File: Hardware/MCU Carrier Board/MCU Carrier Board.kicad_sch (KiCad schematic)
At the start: 0 parts

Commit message: start
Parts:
- added J7, J8: Conn_02x10_Counter_Clockwise, MCU_Controller:HRS_DF40C-20DP-0.4V_51_, symbol MCU_Controller:DF40C-20DP-0.4V_51_
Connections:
- new net GND: J7.12, J7.14, J7.16, J8.16, J8.18, J8.20
- new net GPIO1: J8.11
- new net GPIO10: J7.11
- new net GPIO11: J7.9
- new net GPIO12: J7.7
- new net GPIO13: J7.5
- new net GPIO14: J7.3
- new net GPIO15: J8.10
- new net GPIO16: J8.12
- new net GPIO17: J8.14
- new net GPIO18: J7.19
- new net GPIO2: J8.9
- new net GPIO21: J7.1
- new net GPIO3: J7.15
- new net GPIO35: J8.2
- new net GPIO36: J8.4
- new net GPIO37: J8.6
- new net GPIO38: J8.8
- new net GPIO4: J8.13
- new net GPIO41: J8.1
- new net GPIO42: J8.3
- new net GPIO47: J7.4
- new net GPIO48: J7.2
- new net GPIO5: J8.15
- new net GPIO6: J8.17
- new net GPIO7: J8.19
- new net GPIO8: J7.17
- new net GPIO9: J7.13
- new net RXD0: J8.5
- new net TXD0: J8.7
- new net VCC_3V3: J7.10, J7.6, J7.8
- new net VCC_5V: J7.18, J7.20

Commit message: update
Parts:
- added C1, C3: .1uF, Capacitor_SMD:C_0603_1608Metric_Pad1.08x0.95mm_HandSolder, symbol Device:C
- added C10, C11, C12, C9: 1uF, Capacitor_SMD:C_0603_1608Metric_Pad1.08x0.95mm_HandSolder, symbol Device:C
- added C2, C4: 10uF, Capacitor_SMD:C_0603_1608Metric_Pad1.08x0.95mm_HandSolder, symbol Device:C
- added D4, D5, D6, D7: LED, LED_SMD:LED_0603_1608Metric_Pad1.05x0.95mm_HandSolder, symbol MCU_Controller:LED
- added J2: Conn_01x05_Pin, Connector_JST:JST_EH_S5B-EH_1x05_P2.50mm_Horizontal, symbol MCU_Controller:Conn_01x05_Pin
- added R10, R7, R8, R9: 1K, Resistor_SMD:R_0603_1608Metric_Pad0.98x0.95mm_HandSolder, symbol MCU_Controller:R
- added SW1, SW2, SW3: SW_Push, Button_Switch_SMD:SW_Push_1P1T_XKB_TS-1187A, symbol MCU_Controller:SW_Push
- added SW10, SW11, SW12, SW13, SW14, SW15, SW16, SW5, SW6, SW7, SW8, SW9: SW_Push, Button_Switch_THT:SW_PUSH_6mm, symbol Switch:SW_Push
- added U3: Left Joystick, COM_09032:XDCR_COM-09032, symbol COM-09032:Joystick-09032
- added U4: Right Joystick, COM_09032:XDCR_COM-09032, symbol COM-09032:Joystick-09032
- J7: value Conn_02x10_Counter_Clockwise -> Top Connector; footprint MCU_Controller:HRS_DF40C-20DP-0.4V_51_ -> DF40C:HRS_DF40C-20DS-0.4V_51_; symbol MCU_Controller:DF40C-20DP-0.4V_51_ -> DF40C:DF40C-20DS-0.4V_51_; MANUFACTURER Hirose Electric -> HRS; MAXIMUM_PACKAGE_HEIGHT 1.29mm -> 1.65 mm; PARTREV 02/2020 -> Sept.1.2020
- J8: value Conn_02x10_Counter_Clockwise -> Bottom Connector; footprint MCU_Controller:HRS_DF40C-20DP-0.4V_51_ -> DF40C:HRS_DF40C-20DS-0.4V_51_; symbol MCU_Controller:DF40C-20DP-0.4V_51_ -> DF40C:DF40C-20DS-0.4V_51_; MANUFACTURER Hirose Electric -> HRS; MAXIMUM_PACKAGE_HEIGHT 1.29mm -> 1.65 mm; PARTREV 02/2020 -> Sept.1.2020
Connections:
- net GND: now also J7.11, J7.13, J7.15, J8.15, J8.17, J8.19, C1.1, C10.2, C11.2, C12.2, C2.1, C3.2, C4.2, C9.2, D4.1 (K), D5.1 (K), D6.1 (K), D7.1 (K), J2.3 (Pin_3), SW1.1, SW10.2, SW11.1, SW12.1, SW13.2, SW14.2, SW15.1, SW16.1, SW2.1, SW3.1, SW5.2, SW6.2, SW7.1, SW8.1, SW9.2, U3.B2A (SEL-), U3.H3 (H-), U3.S1 (SHIELD), U3.S2 (SHIELD__1), U3.S3 (SHIELD__2), U3.S4 (SHIELD__3), U3.V3 (V-), U4.B2A (SEL-), U4.H3 (H-), U4.S1 (SHIELD), U4.S2 (SHIELD__1), U4.S3 (SHIELD__2), U4.S4 (SHIELD__3), U4.V3 (V-); no longer J7.12, J7.14, J7.16, J8.16, J8.18, J8.20
- net GPIO1: now also J8.12, C11.1, U4.V2 (V); no longer J8.11
- net GPIO10: now also J7.12, SW16.2; no longer J7.11
- net GPIO11: now also J7.10, SW5.1; no longer J7.9
- net GPIO12: now also J7.8, SW6.1; no longer J7.7
- net GPIO13: now also J7.6, SW7.2; no longer J7.5
- net GPIO14: now also J7.4, SW8.2; no longer J7.3
- net GPIO15: now also J8.9, U4.B1A (SEL+); no longer J8.10
- net GPIO16: now also J8.11, U3.B1A (SEL+); no longer J8.12
- net GPIO17: now also J8.13, SW11.2; no longer J8.14
- net GPIO18: now also J7.20, SW9.1; no longer J7.19
- net GPIO2: now also J8.10, C12.1, U4.H2 (H); no longer J8.9
- net GPIO21: now also J7.2, SW1.2; no longer J7.1
- net GPIO3: now also J7.16, SW12.2; no longer J7.15
- net GPIO35: now also J8.1, R10.1; no longer J8.2
- net GPIO36: now also J8.3, R9.1; no longer J8.4
- net GPIO37: now also J8.5, R8.1; no longer J8.6
- net GPIO38: now also J8.7, R7.1; no longer J8.8
- net GPIO4: now also J8.14, C9.1, U3.V2 (V); no longer J8.13
- net GPIO41: now also J8.2, J2.5 (Pin_5); no longer J8.1
- net GPIO42: now also J8.4, J2.4 (Pin_4); no longer J8.3
- net GPIO47: now also J7.3, SW2.2; no longer J7.4
- net GPIO48: now also J7.1, SW3.2; no longer J7.2
- net GPIO5: now also J8.16, C10.1, U3.H2 (H); no longer J8.15
- net GPIO6: now also J8.18, SW10.1; no longer J8.17
- net GPIO7: now also J8.20, SW13.1; no longer J8.19
- net GPIO8: now also J7.18, SW15.2; no longer J7.17
- net GPIO9: now also J7.14, SW14.1; no longer J7.13
- net RXD0: now also J8.6, J2.2 (Pin_2); no longer J8.5
- net TXD0: now also J8.8, J2.1 (Pin_1); no longer J8.7
- net VCC_3V3: now also J7.5, J7.7, J7.9, C3.1, C4.1, U3.H1 (H+), U3.V1 (V+), U4.H1 (H+), U4.V1 (V+); no longer J7.10, J7.6, J7.8
- net VCC_5V: now also J7.17, J7.19, C1.2, C2.2; no longer J7.18, J7.20
- new net: D5.2 (A), R8.2
- new net: D6.2 (A), R9.2
- new net: D4.2 (A), R7.2
- new net: D7.2 (A), R10.2
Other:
- note added: "I2C"
- note added: "Play Inicater LEDs"
- note added: "Uart"

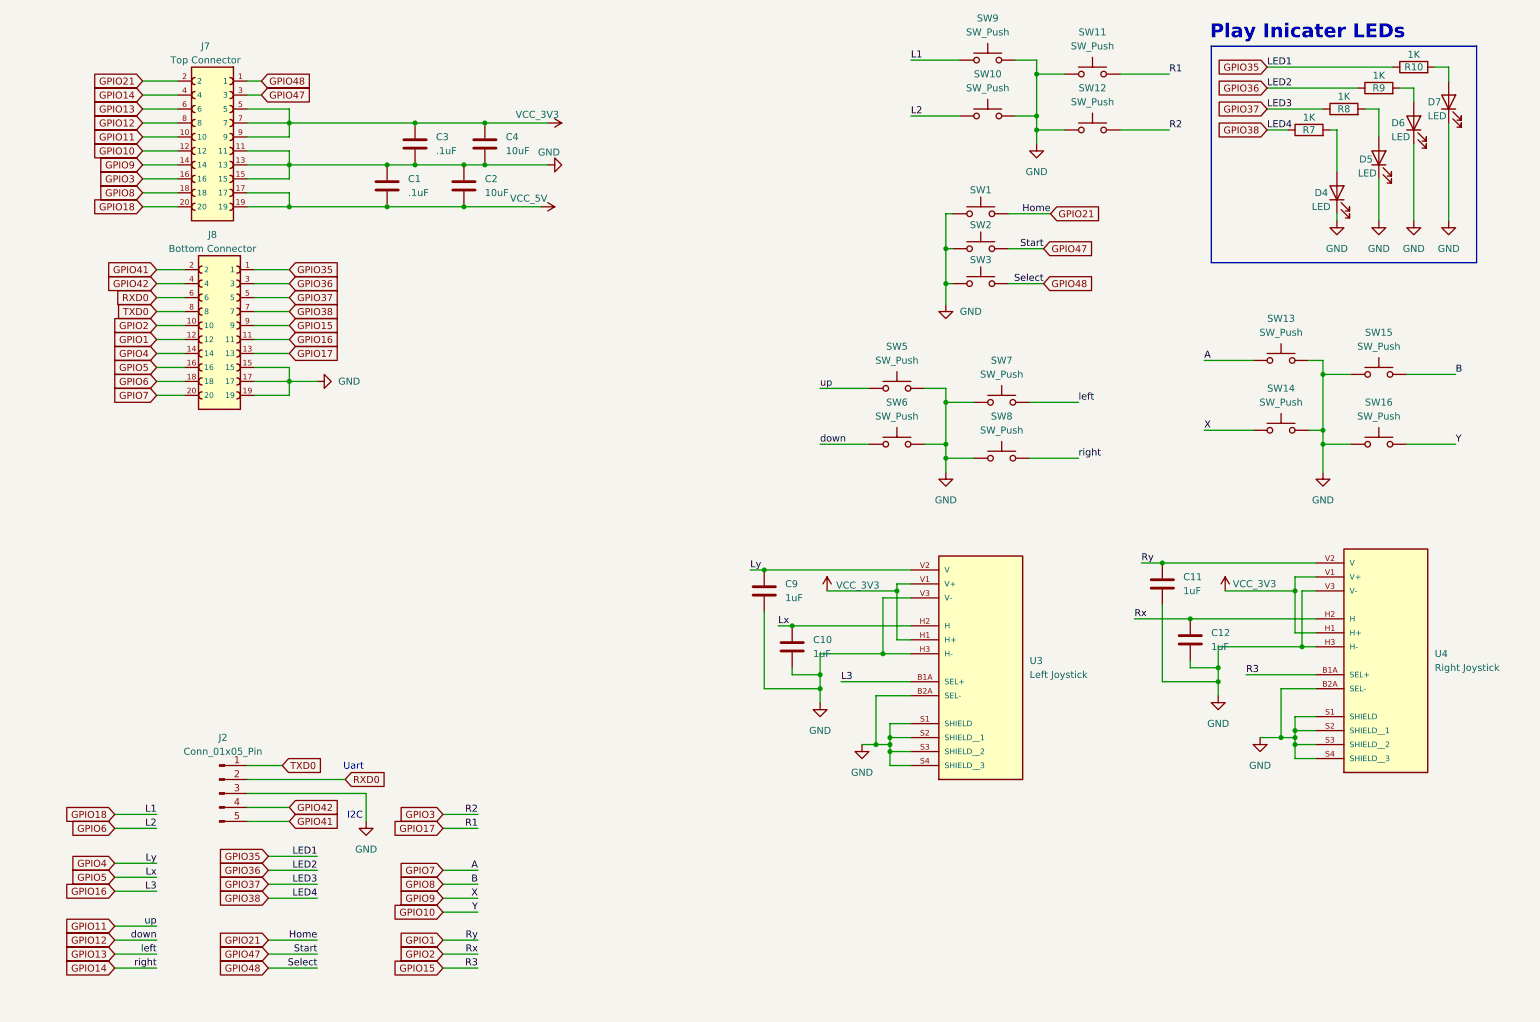
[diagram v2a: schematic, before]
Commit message: locked placement of key components
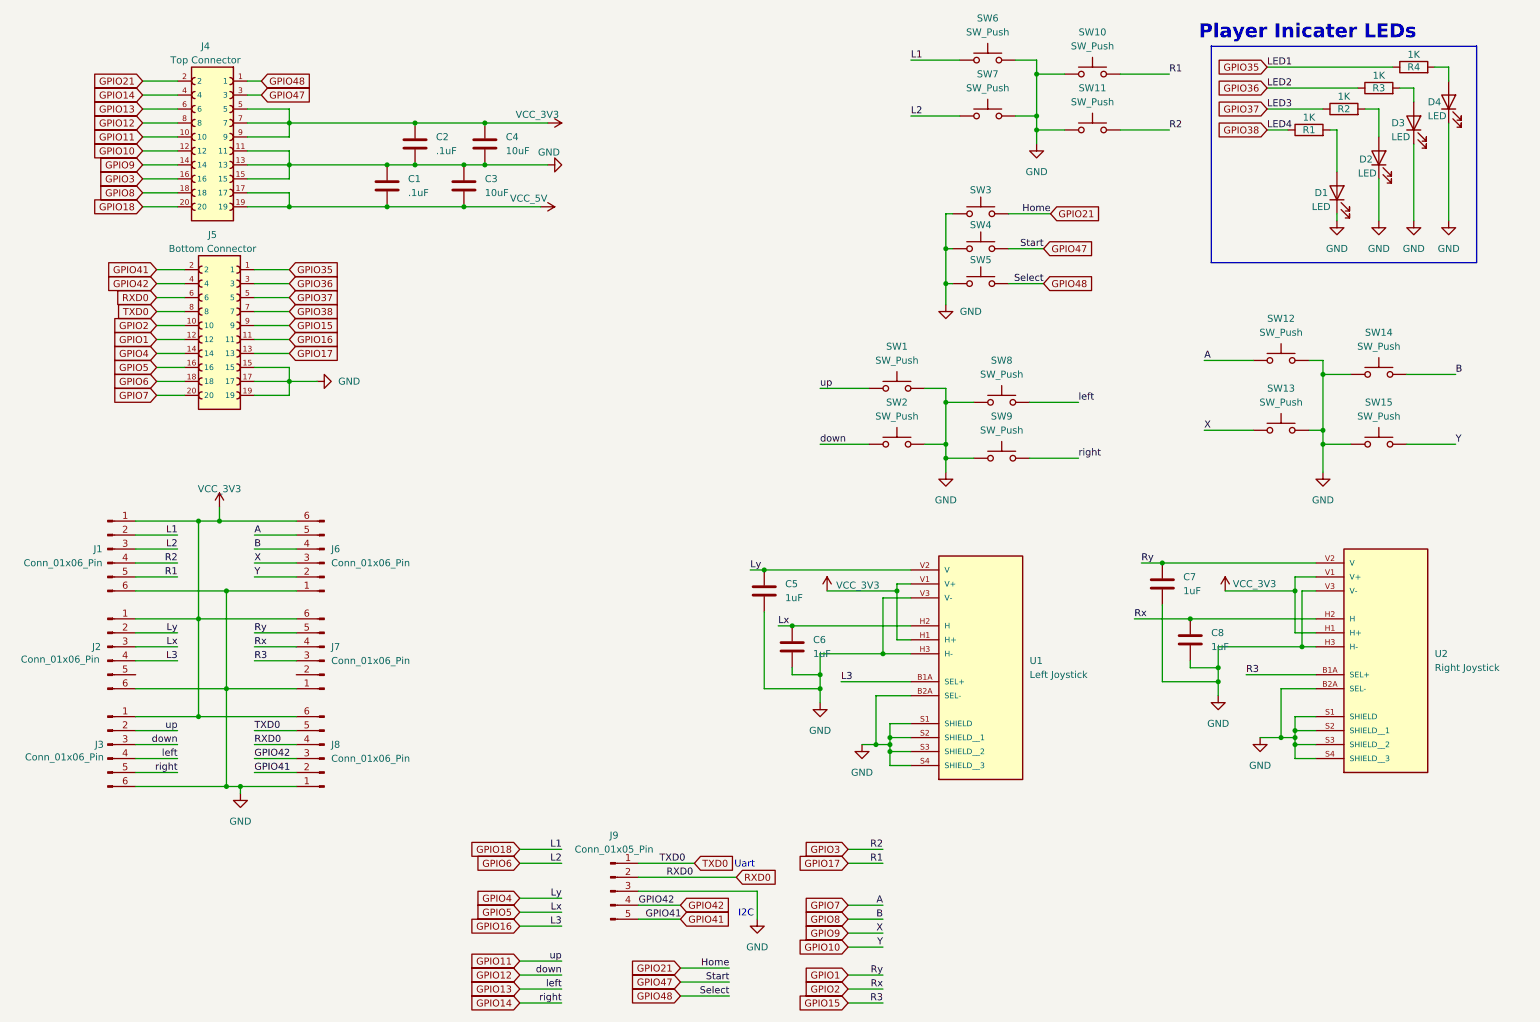
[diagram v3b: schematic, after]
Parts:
- added J1, J2, J3, J6, J7, J8: Conn_01x06_Pin, Connector_PinHeader_1.27mm:PinHeader_1x06_P1.27mm_Vertical, symbol Connector:Conn_01x06_Pin
- C5: renamed from C9; now left out of the parts list
- C6: renamed from C10; now left out of the parts list
- C7: renamed from C11; now left out of the parts list
- C8: renamed from C12; now left out of the parts list
- J9: renamed from J2; now left out of the parts list
- SW1: renamed from SW5; now left out of the parts list
- SW10: renamed from SW11; now left out of the parts list
- SW11: renamed from SW12; now left out of the parts list
- SW12: renamed from SW13; now left out of the parts list
- SW13: renamed from SW14; now left out of the parts list
- SW14: renamed from SW15; now left out of the parts list
- SW15: renamed from SW16; now left out of the parts list
- SW2: renamed from SW6; now left out of the parts list
- SW3: renamed from SW1; now left out of the parts list
- SW4: renamed from SW2; now left out of the parts list
- SW5: renamed from SW3; now left out of the parts list
- SW6: renamed from SW9; now left out of the parts list
- SW7: renamed from SW10; now left out of the parts list
- SW8: renamed from SW7; now left out of the parts list
- SW9: renamed from SW8; now left out of the parts list
- U1: renamed from U3; now left out of the parts list
- U2: renamed from U4; now left out of the parts list
- renumbered C3 to C2, C2 to C3, D4 to D1, D5 to D2, D6 to D3, D7 to D4, J7 to J4, J8 to J5, R7 to R1, R8 to R2, R9 to R3, R10 to R4
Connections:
- net GND: now also J1.6 (Pin_6), J2.6 (Pin_6), J3.6 (Pin_6), J6.1 (Pin_1), J7.1 (Pin_1), J8.1 (Pin_1)
- net GPIO1: now also J7.5 (Pin_5)
- net GPIO10: now also J6.2 (Pin_2)
- net GPIO11: now also J3.2 (Pin_2)
- net GPIO12: now also J3.3 (Pin_3)
- net GPIO13: now also J3.4 (Pin_4)
- net GPIO14: now also J3.5 (Pin_5)
- net GPIO15: now also J7.3 (Pin_3)
- net GPIO16: now also J2.4 (Pin_4)
- net GPIO17: now also J1.5 (Pin_5)
- net GPIO18: now also J1.2 (Pin_2)
- net GPIO2: now also J7.4 (Pin_4)
- net GPIO3: now also J1.4 (Pin_4)
- net GPIO4: now also J2.2 (Pin_2)
- net GPIO41: now also J8.2 (Pin_2)
- net GPIO42: now also J8.3 (Pin_3)
- net GPIO5: now also J2.3 (Pin_3)
- net GPIO6: now also J1.3 (Pin_3)
- net GPIO7: now also J6.5 (Pin_5)
- net GPIO8: now also J6.4 (Pin_4)
- net GPIO9: now also J6.3 (Pin_3)
- net RXD0: now also J8.4 (Pin_4)
- net TXD0: now also J8.5 (Pin_5)
- net VCC_3V3: now also J1.1 (Pin_1), J2.1 (Pin_1), J3.1 (Pin_1), J6.6 (Pin_6), J7.6 (Pin_6), J8.6 (Pin_6)
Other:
- note added: "Player Inicater LEDs"
- note removed: "Play Inicater LEDs"
- moved on the sheet: J9

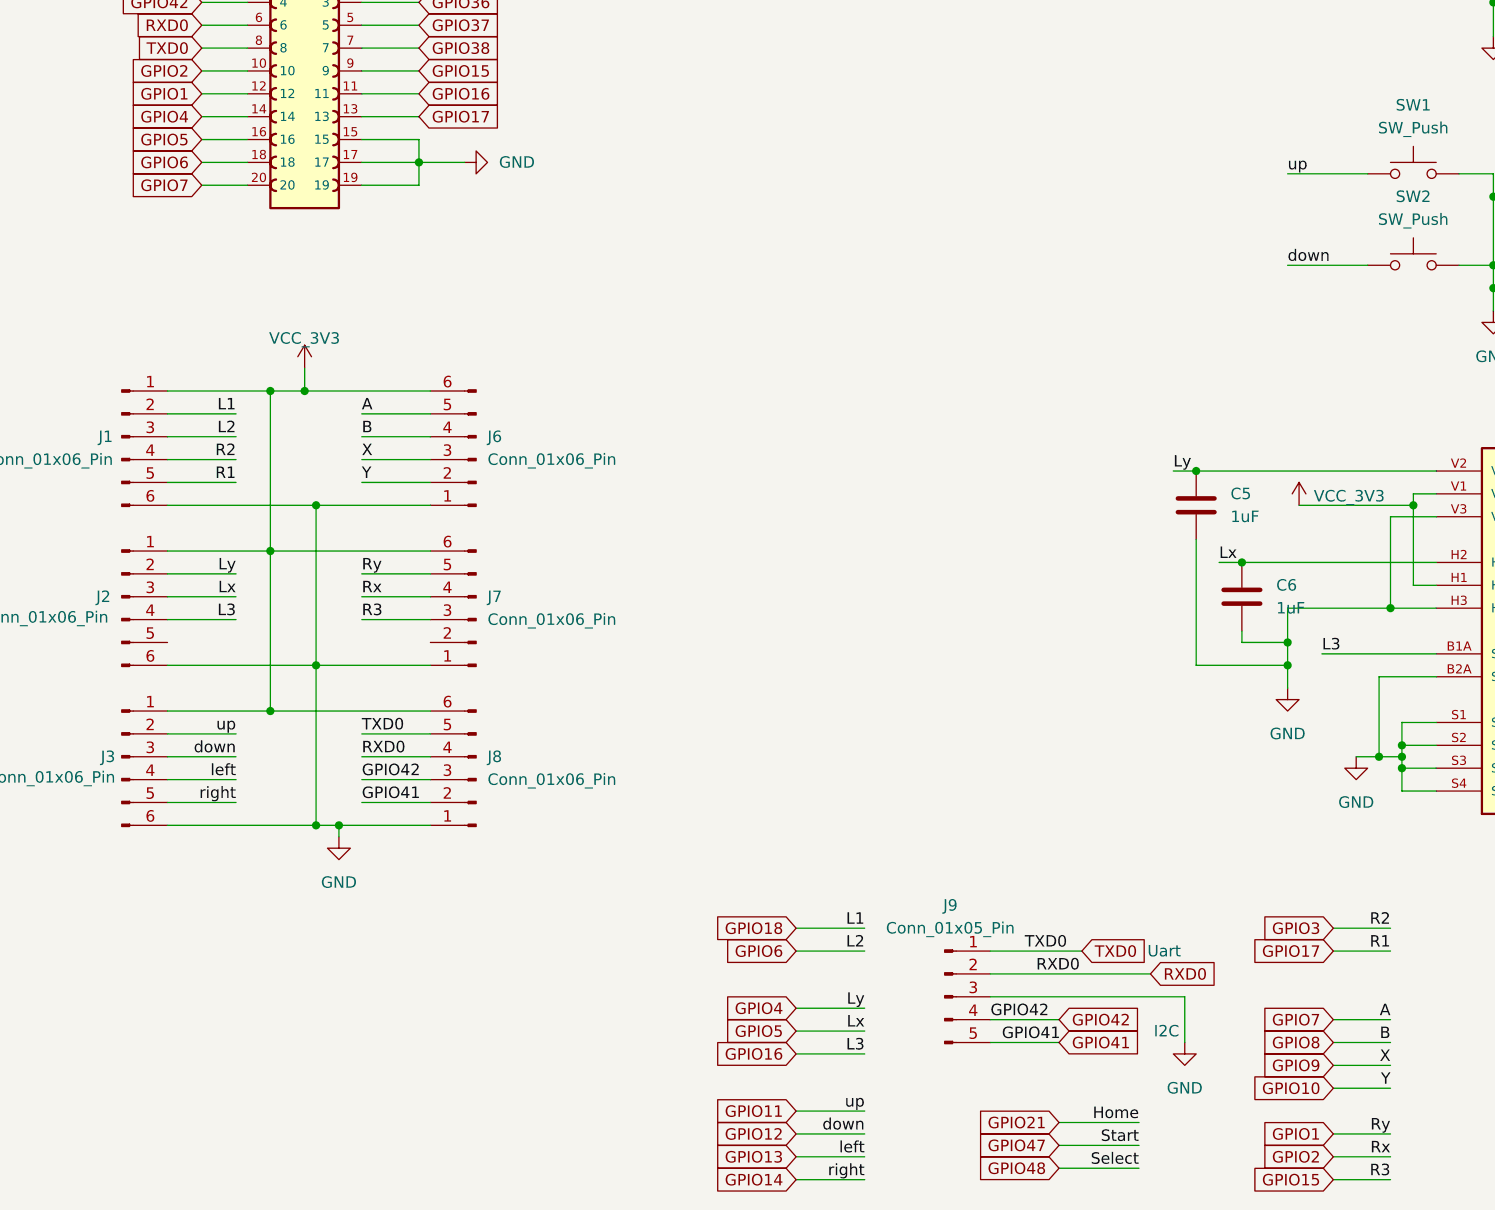
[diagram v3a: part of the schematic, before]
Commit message: reconfigured pins and started routing
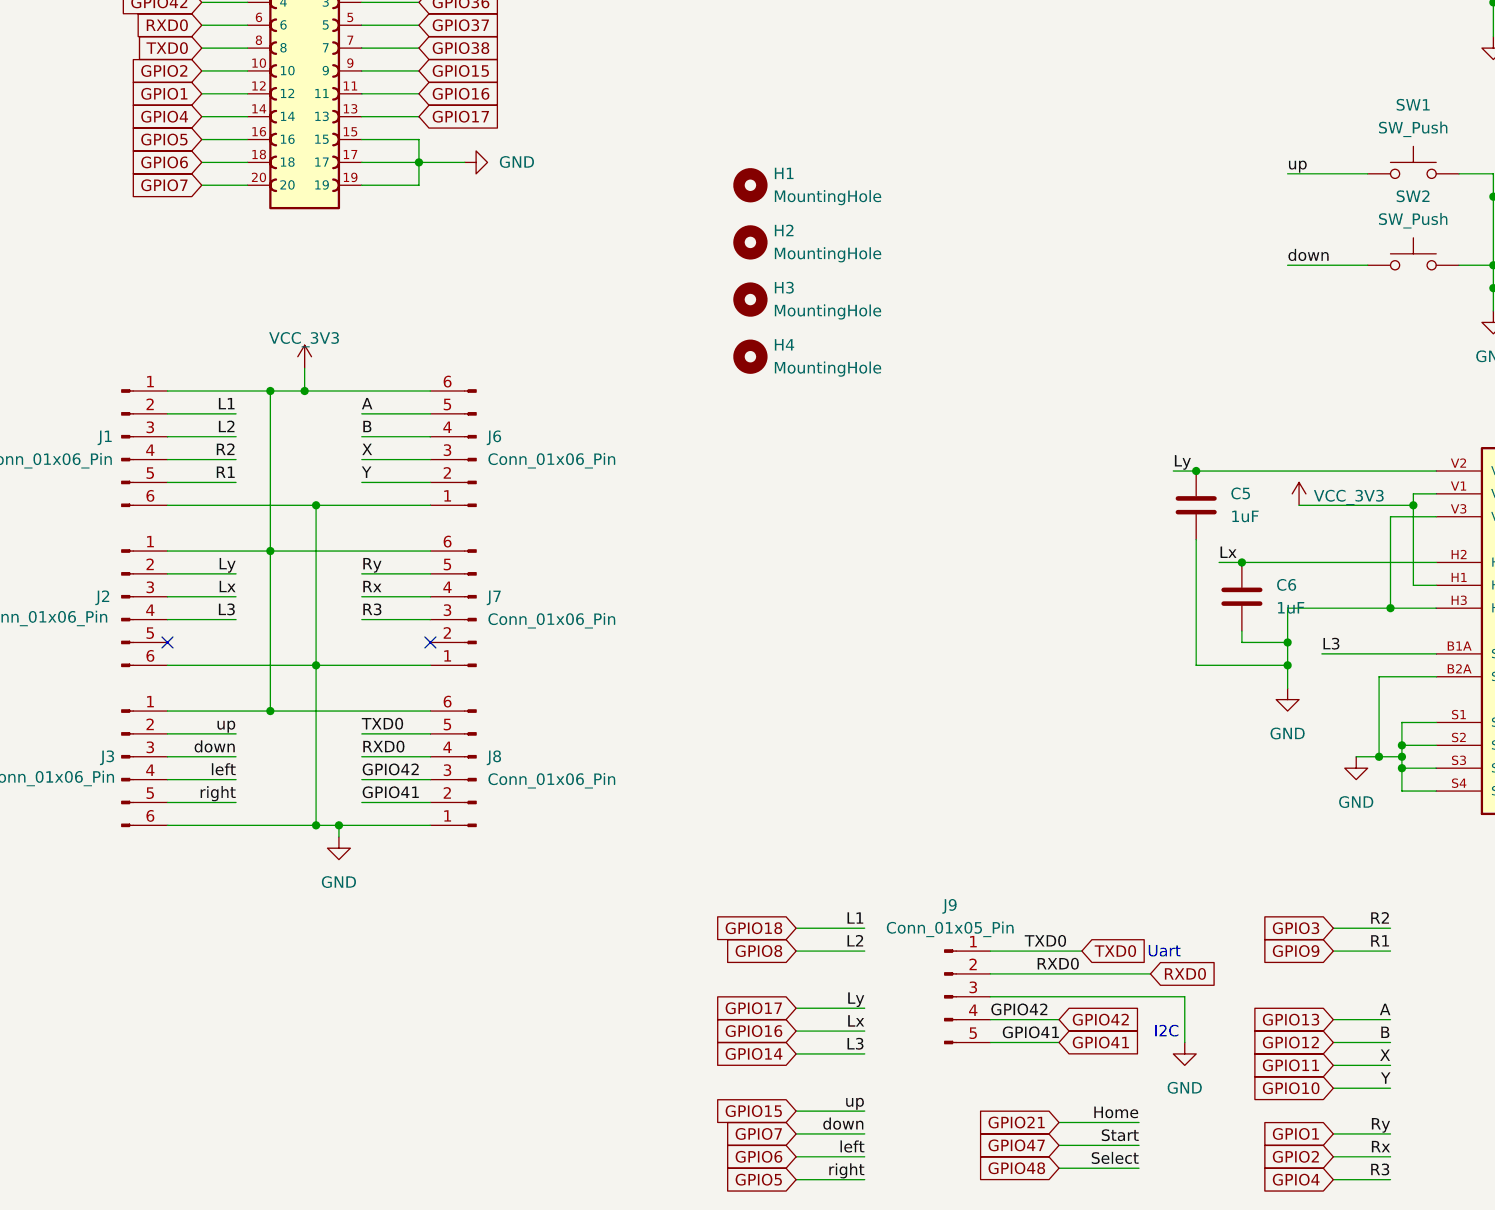
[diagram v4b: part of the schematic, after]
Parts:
- added H1, H2, H3, H4: MountingHole, MountingHole:MountingHole_2.5mm, symbol Mechanical:MountingHole
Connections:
- net GPIO11: now also J6.3 (Pin_3), SW13.1; no longer J3.2 (Pin_2), SW1.1
- net GPIO12: now also J6.4 (Pin_4), SW14.2; no longer J3.3 (Pin_3), SW2.1
- net GPIO13: now also J6.5 (Pin_5), SW12.1; no longer J3.4 (Pin_4), SW8.2
- net GPIO14: now also J2.4 (Pin_4), U1.B1A (SEL+); no longer J3.5 (Pin_5), SW9.2
- net GPIO15: now also J3.2 (Pin_2), SW1.1; no longer J7.3 (Pin_3), U2.B1A (SEL+)
- net GPIO16: now also C6.1, J2.3 (Pin_3), U1.H2 (H); no longer J2.4 (Pin_4), U1.B1A (SEL+)
- net GPIO17: now also C5.1, J2.2 (Pin_2), U1.V2 (V); no longer J1.5 (Pin_5), SW10.2
- net GPIO4: now also J7.3 (Pin_3), U2.B1A (SEL+); no longer C5.1, J2.2 (Pin_2), U1.V2 (V)
- net GPIO5: now also J3.5 (Pin_5), SW9.2; no longer C6.1, J2.3 (Pin_3), U1.H2 (H)
- net GPIO6: now also J3.4 (Pin_4), SW8.2; no longer J1.3 (Pin_3), SW7.1
- net GPIO7: now also J3.3 (Pin_3), SW2.1; no longer J6.5 (Pin_5), SW12.1
- net GPIO8: now also J1.3 (Pin_3), SW7.1; no longer J6.4 (Pin_4), SW14.2
- net GPIO9: now also J1.5 (Pin_5), SW10.2; no longer J6.3 (Pin_3), SW13.1
- no-connect marks 0 -> 2
